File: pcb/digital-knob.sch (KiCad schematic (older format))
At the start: 28 parts, among them IC1 ATTINY20-X, P1 CONN_02X02

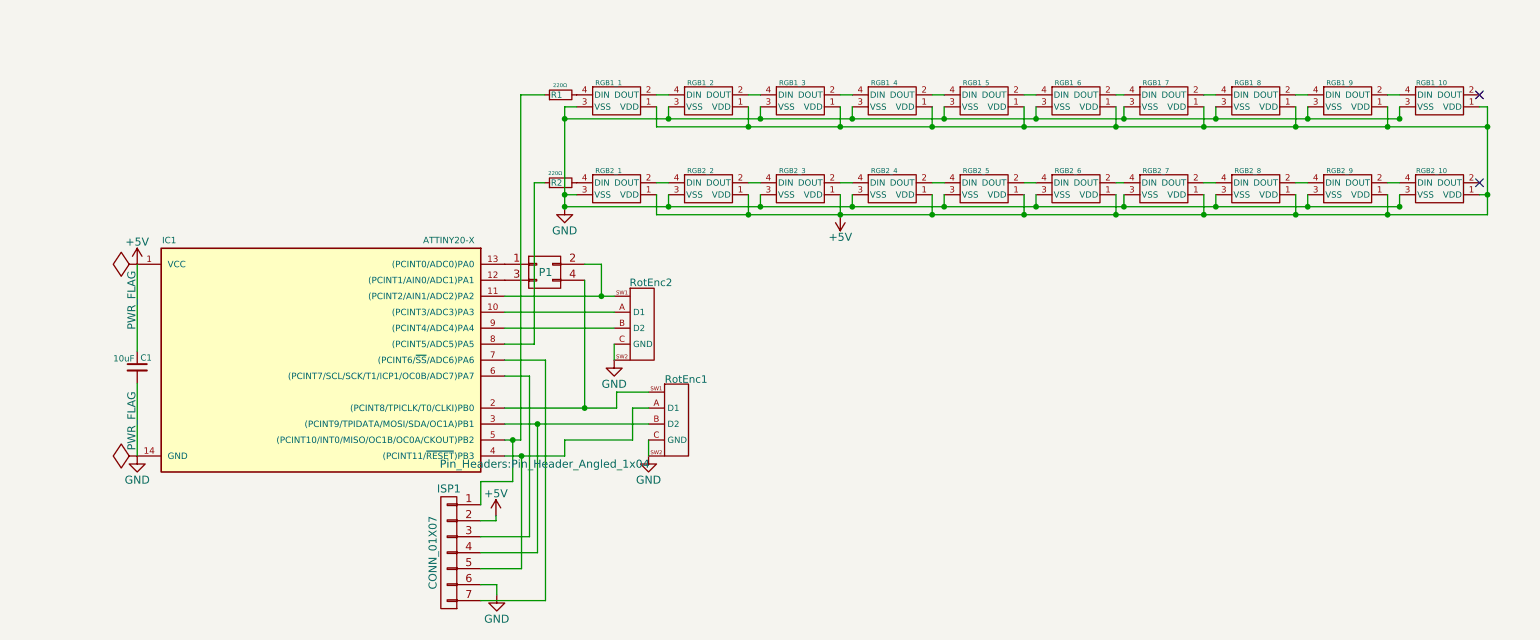
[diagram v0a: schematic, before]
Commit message: Initial version of v2 single encoder pcb
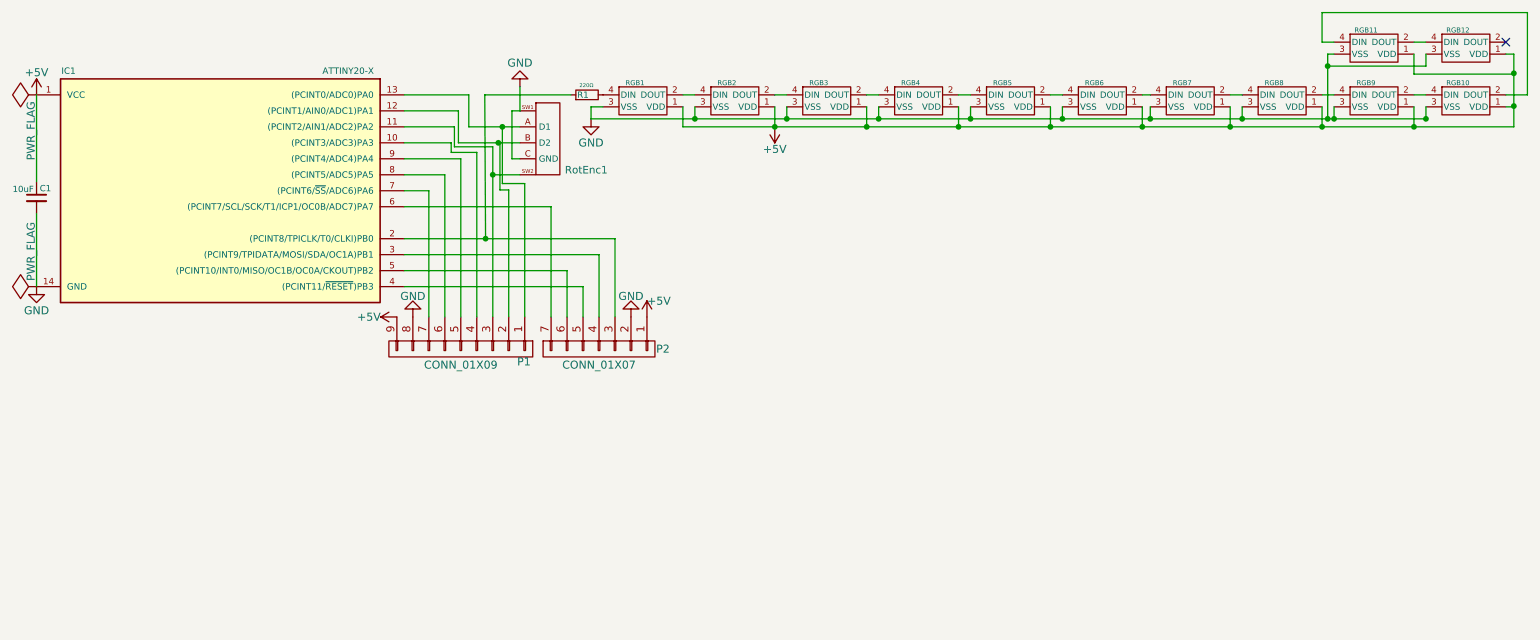
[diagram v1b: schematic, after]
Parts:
- removed ISP1: CONN_01X07, Pin_Headers:Pin_Header_Angled_1x07, symbol CONN_01X07
- removed P1: CONN_02X02, Pin_Headers:Pin_Header_Angled_1x04, symbol CONN_02X02
- removed R2: 220Ω, Resistors_SMD:R_1206, symbol R_Small
- removed RGB2_1, RGB2_10, RGB2_2, RGB2_3, RGB2_4, RGB2_5, RGB2_6, RGB2_7, RGB2_8, RGB2_9: RGB_LED_5050, LEDs:LED_WS2812B-PLCC4, symbol RGB_LED_5050
- removed RotEnc2: Rotary_Encoder, Rotary Encoders:ALPS_STEC12E08, symbol Rotary_Encoder
- added P1: CONN_01X09, symbol CONN_01X09
- added P2: CONN_01X07, symbol CONN_01X07
- added RGB11, RGB12: RGB_LED_5050, LEDs:LED_WS2812B-PLCC4, symbol RGB_LED_5050
- renumbered RGB1_1 to RGB1, RGB1_10 to RGB10, RGB1_2 to RGB2, RGB1_3 to RGB3, RGB1_4 to RGB4, RGB1_5 to RGB5, RGB1_6 to RGB6, RGB1_7 to RGB7, RGB1_8 to RGB8, RGB1_9 to RGB9
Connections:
- net +5V: now also P1.9 (P9), P2.1 (P1), RGB11.1 (VDD), RGB12.1 (VDD)
- net GND: now also RotEnc1.SW1, P1.8 (P8), P2.2 (P2), RGB11.3 (VSS), RGB12.3 (VSS); no longer RotEnc1.SW2
- net at IC1.10 ((PCINT3/ADC3)PA3): now also P1.4 (P4)
- net at IC1.11 ((PCINT2/AIN1/ADC2)PA2): now also RotEnc1.SW2, P1.3 (P3)
- net at IC1.12 ((PCINT1/AIN0/ADC1)PA1): now also RotEnc1.B (D2), P1.2 (P2)
- net at IC1.13 ((PCINT0/ADC0)PA0): now also RotEnc1.A (D1), P1.1 (P1)
- net at IC1.2 ((PCINT8/TPICLK/T0/CLKI)PB0): now also R1.1, P2.3 (P3); no longer RotEnc1.SW1
- net at IC1.3 ((PCINT9/TPIDATA/MOSI/SDA/OC1A)PB1): now also P2.4 (P4); no longer RotEnc1.B (D2)
- net at IC1.4 ((PCINT11/~RESET~)PB3): now also P2.5 (P5); no longer RotEnc1.A (D1)
- net at IC1.5 ((PCINT10/INT0/MISO/OC1B/OC0A/CKOUT)PB2): now also P2.6 (P6); no longer R1.1
- net at IC1.6 ((PCINT7/SCL/SCK/T1/ICP1/OC0B/ADC7)PA7): now also P2.7 (P7)
- net at IC1.7 ((PCINT6/~SS~/ADC6)PA6): now also P1.7 (P7)
- net at IC1.8 ((PCINT5/ADC5)PA5): now also P1.6 (P6)
- net at IC1.9 ((PCINT4/ADC4)PA4): now also P1.5 (P5)
- net at RGB10.2 (DOUT): now also RGB11.4 (DIN)
- new net: RGB11.2 (DOUT), RGB12.4 (DIN)
- no-connect marks 2 -> 1
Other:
- moved on the sheet: C1, IC1, R1, RGB1, RGB10, RGB2, RGB3, RGB4, RGB5, RGB6, RGB7, RGB8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
